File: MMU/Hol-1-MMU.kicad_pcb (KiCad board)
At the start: 2 copper layers, 106.7 x 76.2 mm, 35 parts, among them P1 DATA BUS, P2 ADDRESS PORT, P3 DATA PORT, P4 MMU CONTROL, P5 Power, SW1 HEX_SWITCH, SW2 HEX_SWITCH, SW3 HEX_SWITCH, SW4 HEX_SWITCH, SW5 DPDT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

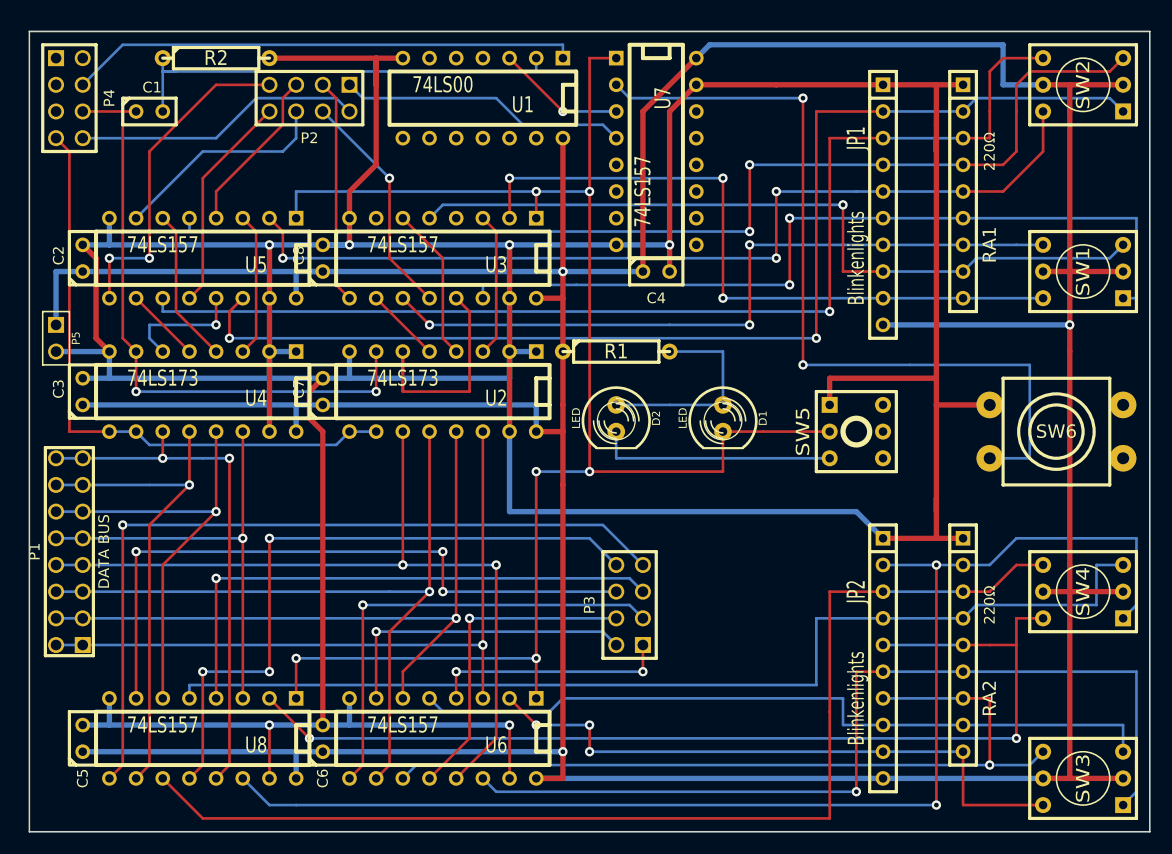
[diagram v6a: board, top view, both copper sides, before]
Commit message: v1.5.8 MMU added blinkenlights to display memory address register
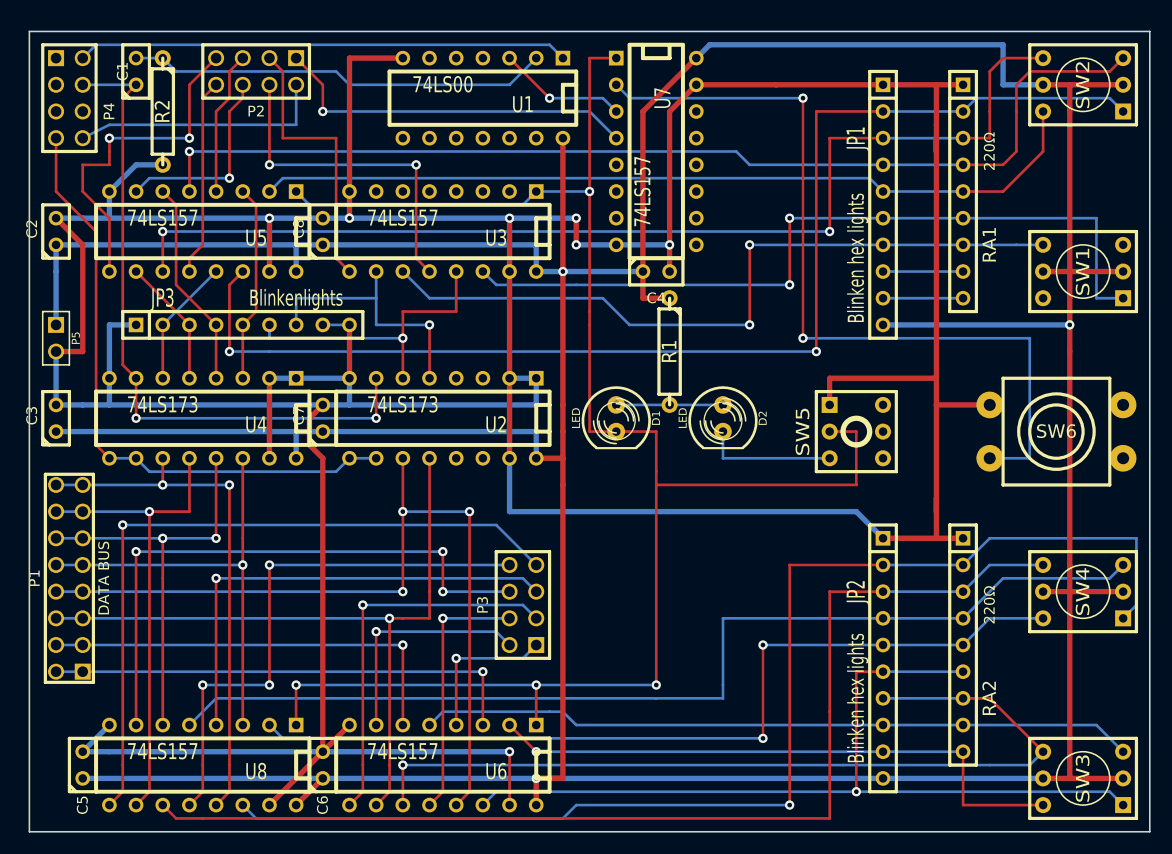
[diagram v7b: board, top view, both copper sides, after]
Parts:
- added JP3: Blinkenlights, SIL-9, F.Cu at (124.5, 91.4)
- JP1, JP2: value Blinkenlights -> Blinken hex lights
- moved D1 10.2 mm to (160.0, 100.3)
- moved D2 10.2 mm to (170.2, 100.3)
- moved P3 10.2 mm to (151.1, 118.1)
- moved R2 7.18 mm to (116.8, 71.1), turned to 270 degrees
- moved P2 5.68 mm to (125.7, 67.3)
- moved R1 5.08 mm to (165.1, 94.0), turned to 270 degrees
- moved C1 4.02 mm to (114.3, 67.3), turned to 90 degrees
- moved C2 3.59 mm to (106.7, 82.5)
- moved C3 3.59 mm to (106.7, 100.3)
- moved C8 2.54 mm to (132.1, 82.5)
- moved U3 2.54 mm to (143.5, 82.5)
- moved U5 2.54 mm to (120.7, 82.5)
- moved C5 2.54 mm to (109.2, 133.3)
- moved C6 2.54 mm to (132.1, 133.3)
- moved C7 2.54 mm to (132.1, 100.3)
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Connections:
- JP1 pad 8: N-0000044 -> N-0000041
- JP1 pad 9: N-0000034 (its old number) -> N-0000042
- P1 pad 1: N-0000049 (its old number) -> N-0000019
- P1 pad 2: N-0000049 (its old number) -> N-0000019
- P1 pad 3: N-0000048 (its old number) -> N-0000020
- P1 pad 4: N-0000048 (its old number) -> N-0000020
- P4 pad 2: (no net) -> /RAM-INPUT
- P4 pad 4: /RAM-INPUT -> /CLK
- P4 pad 6: /CLK -> (no net)
- RA1 pad 8: N-0000044 -> N-0000041
- RA1 pad 9: N-0000034 (its old number) -> N-0000042
- SW1 pad 3: N-0000044 -> (no net)
- SW1 pad 6: N-0000034 (its old number) -> (no net)
- U2 pad 13: N-0000048 (its old number) -> (no net)
- U2 pad 14: N-0000049 (its old number) -> (no net)
- U2 pad 3: N-0000033 -> (no net)
- U2 pad 4: N-0000029 -> (no net)
- U3 pad 2: N-0000034 (its old number) -> (no net)
- U3 pad 3: N-0000033 -> (no net)
- U3 pad 5: N-0000044 -> (no net)
- U3 pad 6: N-0000029 -> (no net)
- U6 pad 3: N-0000049 (its old number) -> N-0000019
- U6 pad 6: N-0000048 (its old number) -> N-0000020
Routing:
- net N-0000044: track 74.0 -> 0.00 mm, vias 1 -> 0
- net N-0000049 (its old number): track 66.0 -> 0.00 mm, vias 1 -> 0
- net N-0000034 (its old number): track 66.0 -> 0.00 mm, vias 3 -> 0
- net N-0000048 (its old number): track 65.6 -> 0.00 mm, vias 1 -> 0
- net N-0000019: track 0.00 -> 45.7 mm, vias 0 -> 1
- net N-0000020: track 0.00 -> 40.6 mm, vias 0 -> 1
- net GND: track 453.6 -> 478.1 mm, vias 6 -> 7
- net N-0000049: track 7.18 -> 25.4 mm, vias 0 -> 1
- net N-0000013: track 99.4 -> 84.1 mm, vias 2 -> 3
- net N-0000029: track 14.8 -> 0.00 mm
- net N-0000033: track 13.8 -> 0.00 mm
- net N-0000063: track 63.8 -> 52.6 mm
- net /PROG: track 154.9 -> 166.2 mm
- net N-0000037: track 22.0 -> 32.3 mm, vias 1 -> 2
- net N-0000068: track 20.3 -> 10.2 mm
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
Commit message: v1.5.9 MMU tie unused inputs to ground
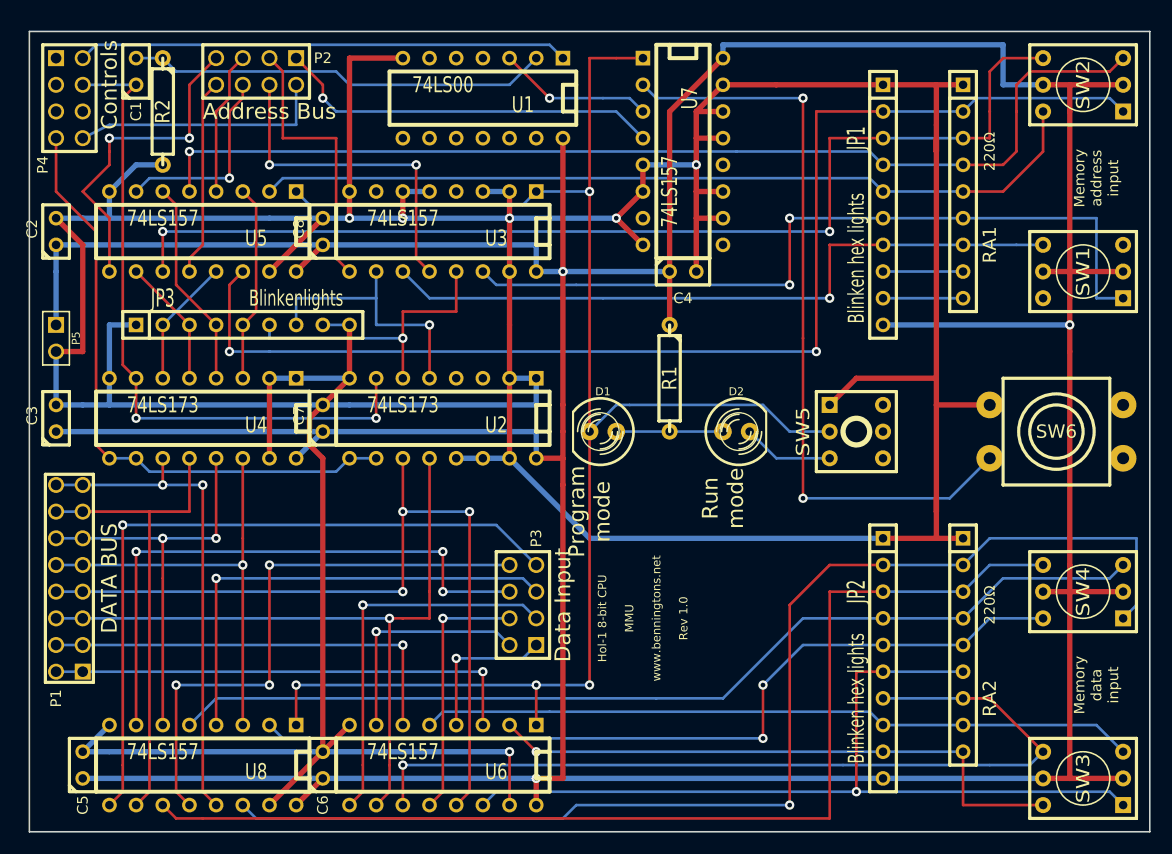
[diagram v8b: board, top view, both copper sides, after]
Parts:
- moved C4 2.54 mm to (166.4, 86.4)
- moved R1 2.54 mm to (165.1, 96.5)
- moved U7 2.54 mm to (166.4, 74.9)
- moved D1 1.80 mm to (158.8, 101.6), turned to 180 degrees
- moved D2 1.80 mm to (171.4, 101.6), turned to 0 degrees
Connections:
- U2 pad 13: (no net) -> GND
- U2 pad 14: (no net) -> GND
- U3 pad 2: (no net) -> GND
- U3 pad 3: (no net) -> GND
- U3 pad 5: (no net) -> GND
- U3 pad 6: (no net) -> GND
- U7 pad 10: (no net) -> GND
- U7 pad 11: (no net) -> GND
- U7 pad 13: (no net) -> GND
- U7 pad 14: (no net) -> GND
- U7 pad 5: (no net) -> GND
- U7 pad 6: (no net) -> GND
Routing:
- net GND: track 478.1 -> 506.8 mm, vias 7 -> 6
- net /PROG: track 166.2 -> 154.3 mm
- net N-0000057: track 78.0 -> 73.2 mm
- net N-0000016: track 99.7 -> 95.2 mm
- net N-000009: track 12.7 -> 8.67 mm
- net N-0000041: track 70.7 -> 67.1 mm, vias 2 -> 1
- net +5V: track 462.2 -> 465.0 mm
- net N-0000056: track 52.6 -> 55.1 mm
- net N-0000058: track 12.3 -> 14.8 mm
- net N-0000054: track 50.1 -> 47.5 mm
- net N-0000019: track 84.1 -> 81.9 mm
- net N-0000017: track 118.2 -> 116.0 mm
- net /RAM-IN: track 35.1 -> 36.9 mm
- net N-000005: track 32.6 -> 31.1 mm
- net N-0000042: vias 1 -> 0
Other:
- board text added: "Address Bus"
- board text added: "Controls"
- board text added: "DATA BUS"
- board text added: "Data Input"
- board text added: "Hol-1 8-bit CPU MMU www.benningtons.net Rev 1.0"
- board text added: "Memory address input"
- board text added: "Memory data input"
- board text added: "Program mode"
- board text added: "Run mode"
